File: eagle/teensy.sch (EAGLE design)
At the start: 3 parts, among them SW2 282834-2

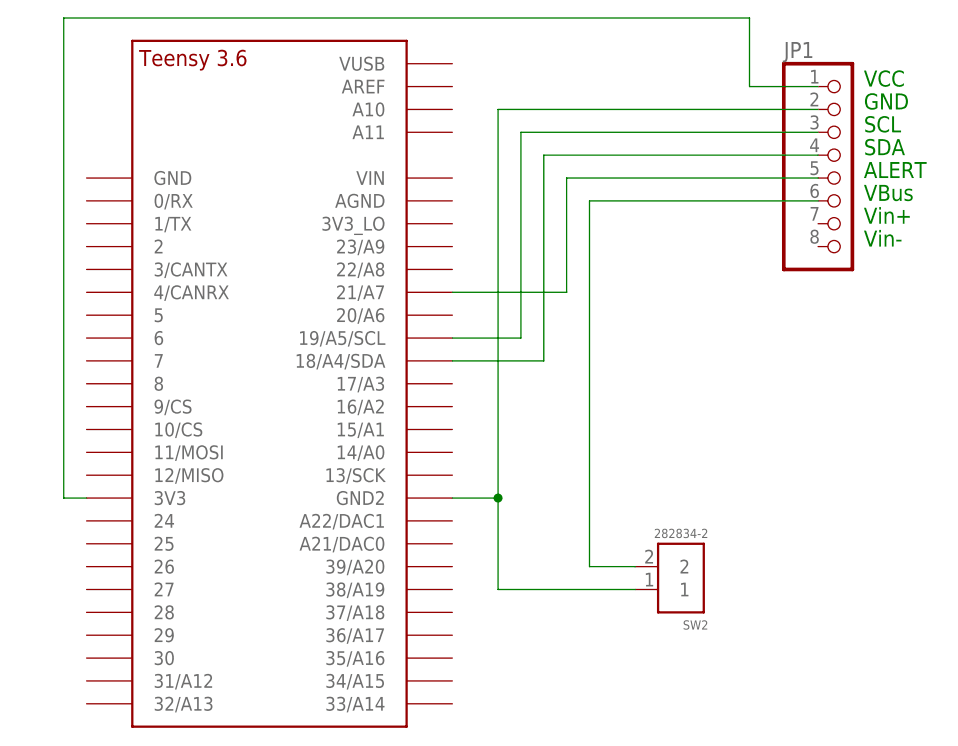
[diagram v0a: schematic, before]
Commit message: update and sync all schematics and images - fix labels and add consistent attribution
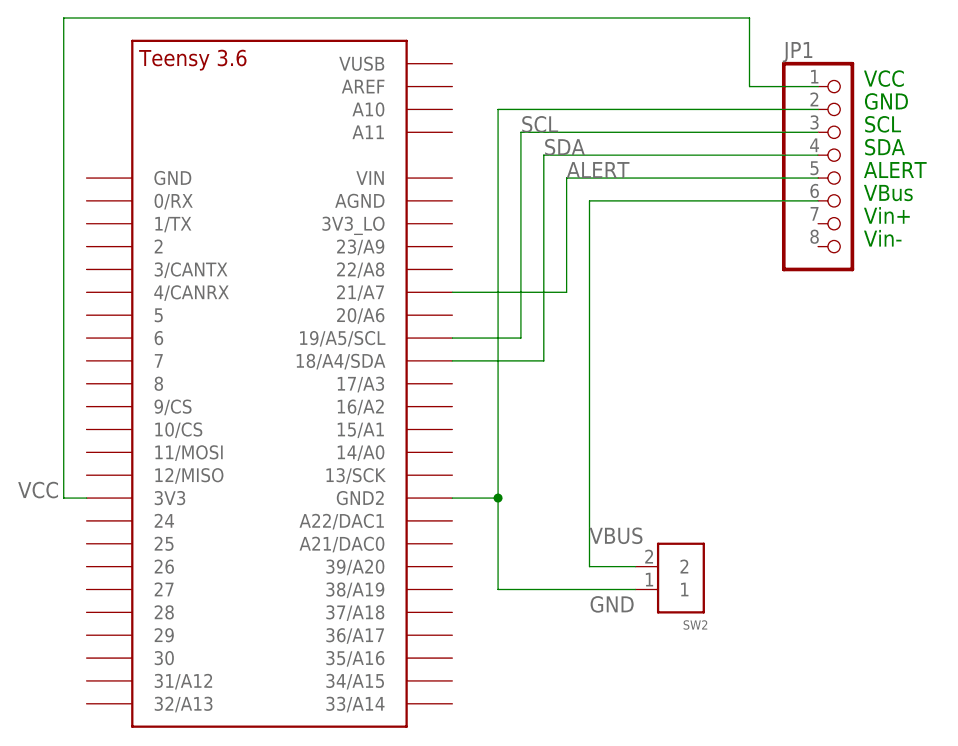
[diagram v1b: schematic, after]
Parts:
- renumbered U$1 to U1
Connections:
- net N$1 renamed VCC
- net N$2 renamed GND
- net N$3 renamed SCL
- net N$4 renamed SDA
- net N$5 renamed ALERT
- net N$8 renamed VBUS
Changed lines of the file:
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@@
 <class number="0" name="default" width="0" drill="0">
+</class>
+<class number="1" name="signal" width="0" drill="0">
+</class>
+<class number="2" name="current" width="0" drill="0">
 </class>
 </classes>
 <parts>
 <part name="JP1" library="pinhead" library_urn="urn:adsk.eagle:library:325" deviceset="PINHD-1X8" device="" package3d_urn="urn:adsk.eagle:package:22409/2"/>
-<part name="SW2" library="282834-2" deviceset="282834-2" device="" override_package3d_urn="urn:adsk.eagle:package:28284809/2" override_package_urn="urn:adsk.eagle:footprint:28284810/1"/>
-<part name="U$1" library="Teensy356" deviceset="TEENSY_3.5/3.6_BASIC" device="" override_package3d_urn="urn:adsk.eagle:package:28291835/2" override_package_urn="urn:adsk.eagle:footprint:28291836/1"/>
+<part name="SW2" library="282834-2" deviceset="282834-2" device="" override_package3d_urn="urn:adsk.eagle:package:28284809/2" override_package_urn="urn:adsk.eagle:footprint:28284810/1" value=""/>
+<part name="U1" library="Teensy356" deviceset="TEENSY_3.5/3.6_BASIC" device="" override_package3d_urn="urn:adsk.eagle:package:28291835/2" override_package_urn="urn:adsk.eagle:footprint:28291836/1"/>
 </parts>
 <sheets>
@@
 <attribute name="VALUE" x="74.17121875" y="72.7781" size="1.01706875" layer="96" rot="R180"/>
 </instance>
-<instance part="U$1" gate="G$1" x="25.4" y="99.06" smashed="yes"/>
+<instance part="U1" gate="G$1" x="25.4" y="99.06" smashed="yes"/>
 </instances>
 <busses>
 </busses>
 <nets>
-<net name="N$1" class="0">
+<net name="VCC" class="0">
 <segment>
-<pinref part="U$1" gate="G$1" pin="3V3"/>
+<pinref part="U1" gate="G$1" pin="3V3"/>
 <wire x1="2.54" y1="76.2" x2="5.08" y2="76.2" width="0.1524" layer="91"/>
 <wire x1="2.54" y1="76.2" x2="2.54" y2="129.54" width="0.1524" layer="91"/>
@@
 <pinref part="JP1" gate="A" pin="1"/>
 <wire x1="78.74" y1="121.92" x2="86.36" y2="121.92" width="0.1524" layer="91"/>
+<label x="-2.54" y="76.2" size="1.778" layer="95"/>
 </segment>
 </net>
-<net name="N$2" class="0">
+<net name="GND" class="0">
 <segment>
 <wire x1="50.8" y1="66.04" x2="50.8" y2="76.2" width="0.1524" layer="91"/>
@@
 <pinref part="SW2" gate="G$1" pin="1"/>
 <wire x1="50.8" y1="66.04" x2="66.04" y2="66.04" width="0.1524" layer="91"/>
-<pinref part="U$1" gate="G$1" pin="GND2"/>
+<pinref part="U1" gate="G$1" pin="GND2"/>
 <wire x1="45.72" y1="76.2" x2="50.8" y2="76.2" width="0.1524" layer="91"/>
 <junction x="50.8" y="76.2"/>
 <pinref part="JP1" gate="A" pin="2"/>
 <wire x1="50.8" y1="119.38" x2="86.36" y2="119.38" width="0.1524" layer="91"/>
+<label x="60.96" y="63.5" size="1.778" layer="95"/>
 </segment>
 </net>
-<net name="N$3" class="0">
+<net name="SCL" class="0">
 <segment>
-<pinref part="U$1" gate="G$1" pin="19/A5/SCL"/>
+<pinref part="U1" gate="G$1" pin="19/A5/SCL"/>
 <wire x1="53.34" y1="93.98" x2="45.72" y2="93.98" width="0.1524" layer="91"/>
 <wire x1="53.34" y1="93.98" x2="53.34" y2="116.84" width="0.1524" layer="91"/>
 <pinref part="JP1" gate="A" pin="3"/>
 <wire x1="53.34" y1="116.84" x2="86.36" y2="116.84" width="0.1524" layer="91"/>
+<label x="53.34" y="116.84" size="1.778" layer="95"/>
 </segment>
 </net>
-<net name="N$4" class="0">
+<net name="SDA" class="0">
 <segment>
-<pinref part="U$1" gate="G$1" pin="18/A4/SDA"/>
+<pinref part="U1" gate="G$1" pin="18/A4/SDA"/>
 <wire x1="45.72" y1="91.44" x2="55.88" y2="91.44" width="0.1524" layer="91"/>
 <pinref part="JP1" gate="A" pin="4"/>
 <wire x1="86.36" y1="114.3" x2="55.88" y2="114.3" width="0.1524" layer="91"/>
 <wire x1="55.88" y1="114.3" x2="55.88" y2="91.44" width="0.1524" layer="91"/>
+<label x="55.88" y="114.3" size="1.778" layer="95"/>
 </segment>
 </net>
-<net name="N$8" class="0">
+<net name="VBUS" class="0">
 <segment>
 <wire x1="60.96" y1="109.22" x2="60.96" y2="68.58" width="0.1524" layer="91"/>
@@
 <pinref part="JP1" gate="A" pin="6"/>
 <wire x1="60.96" y1="109.22" x2="86.36" y2="109.22" width="0.1524" layer="91"/>
+<label x="60.96" y="71.12" size="1.778" layer="95"/>
 </segment>
 </net>
-<net name="N$5" class="0">
+<net name="ALERT" class="0">
 <segment>
 <pinref part="JP1" gate="A" pin="5"/>
 <wire x1="86.36" y1="111.76" x2="58.42" y2="111.76" width="0.1524" layer="91"/>
 <wire x1="58.42" y1="111.76" x2="58.42" y2="99.06" width="0.1524" layer="91"/>
-<pinref part="U$1" gate="G$1" pin="21/A7"/>
+<pinref part="U1" gate="G$1" pin="21/A7"/>
 <wire x1="58.42" y1="99.06" x2="45.72" y2="99.06" width="0.1524" layer="91"/>
+<label x="58.42" y="111.76" size="1.778" layer="95"/>
 </segment>
 </net>
